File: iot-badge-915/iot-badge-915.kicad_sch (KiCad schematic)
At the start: 64 parts, among them J1 USB_C_Receptacle_USB2.0, J2 Wire ANT, J3 Conn_01x04_Male, Q1 BC847, Q2 BC847, Q3 BC847, SW1 SW_Push, SW2 SW_Push, SW3 SW_Push, SW4 SW_Push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

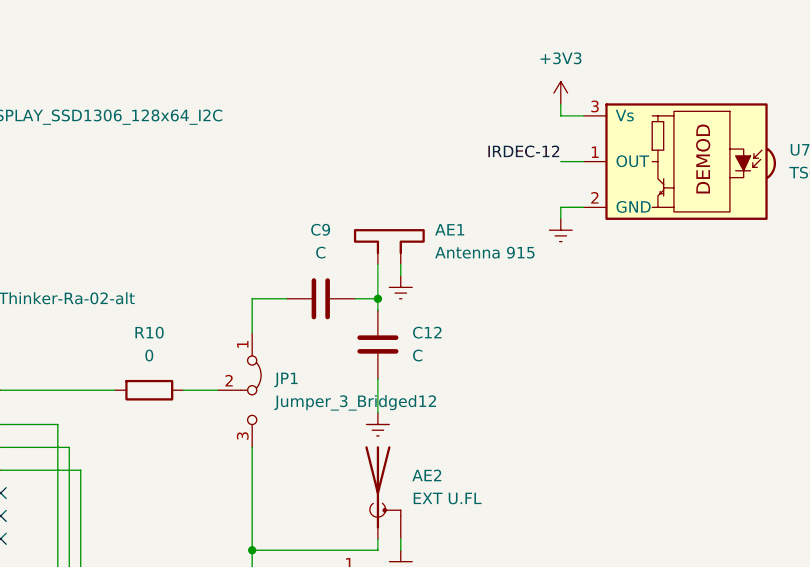
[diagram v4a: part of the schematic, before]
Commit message: added tuning cap an inductor to ant circuit
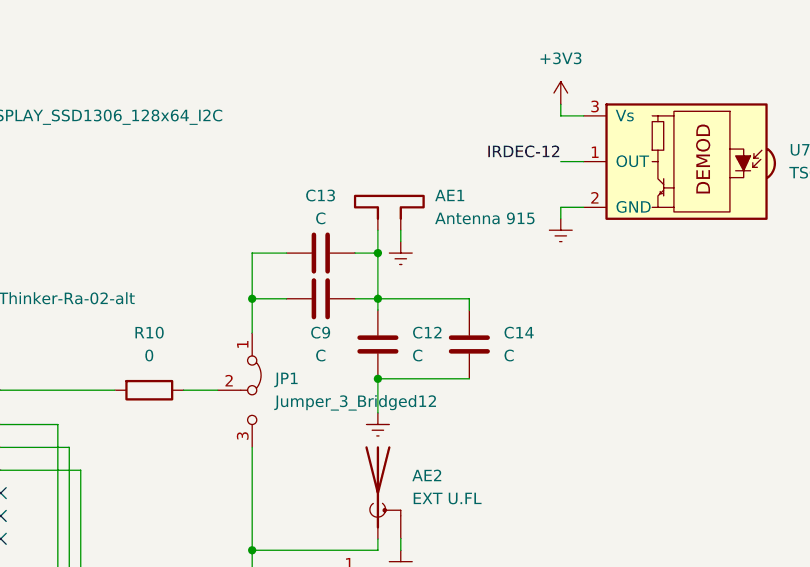
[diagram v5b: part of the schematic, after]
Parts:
- added C13, C14: C, Capacitor_SMD:C_0805_2012Metric_Pad1.18x1.45mm_HandSolder, symbol Device:C
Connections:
- net Earth: now also C14.1
- net at AE1.1, C12.2, C9.1: now also C13.1, C14.2
- net at C9.2, JP1.1 (A): now also C13.2
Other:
- moved on the sheet: AE1
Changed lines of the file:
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@@
   (junction (at 29.21 45.72) (diameter 0) (color 0 0 0 0)
   )
+  (junction (at 167.64 80.01) (diameter 0) (color 0 0 0 0)
+  )
   (junction (at 21.59 45.72) (diameter 0) (color 0 0 0 0)
   )
@@
   (junction (at 26.67 57.15) (diameter 0) (color 0 0 0 0)
   )
+  (junction (at 181.61 74.93) (diameter 0) (color 0 0 0 0)
+  )
   (junction (at 257.81 111.76) (diameter 0) (color 0 0 0 0)
   )
@@
   (junction (at 114.3 55.88) (diameter 0) (color 0 0 0 0)
   )
+  (junction (at 181.61 88.9) (diameter 0) (color 0 0 0 0)
+  )
   (junction (at 218.44 26.67) (diameter 0) (color 0 0 0 0)
   )
@@
     (stroke (width 0) (type default) (color 0 0 0 0))
   )
+  (wire (pts (xy 171.45 74.93) (xy 167.64 74.93))
+    (stroke (width 0) (type default) (color 0 0 0 0))
+  )
   (wire (pts (xy 115.57 185.42) (xy 115.57 189.23))
     (stroke (width 0) (type default) (color 0 0 0 0))
@@
     (stroke (width 0) (type default) (color 0 0 0 0))
   )
+  (wire (pts (xy 191.77 80.01) (xy 191.77 81.28))
+    (stroke (width 0) (type default) (color 0 0 0 0))
+  )
   (wire (pts (xy 115.57 176.53) (xy 118.11 176.53))
     (stroke (width 0) (type default) (color 0 0 0 0))
@@
     (stroke (width 0) (type default) (color 0 0 0 0))
   )
+  (wire (pts (xy 181.61 88.9) (xy 191.77 88.9))
+    (stroke (width 0) (type default) (color 0 0 0 0))
+  )
   (wire (pts (xy 163.83 125.73) (xy 163.83 158.75))
     (stroke (width 0) (type default) (color 0 0 0 0))
@@
     (stroke (width 0) (type default) (color 0 0 0 0))
   )
+  (wire (pts (xy 167.64 74.93) (xy 167.64 80.01))
+    (stroke (width 0) (type default) (color 0 0 0 0))
+  )
   (wire (pts (xy 171.45 80.01) (xy 167.64 80.01))
     (stroke (width 0) (type default) (color 0 0 0 0))
   )
+  (wire (pts (xy 179.07 74.93) (xy 181.61 74.93))
+    (stroke (width 0) (type default) (color 0 0 0 0))
+  )
   (wire (pts (xy 91.44 149.86) (xy 91.44 151.13))
     (stroke (width 0) (type default) (color 0 0 0 0))
   )
-  (wire (pts (xy 181.61 76.2) (xy 181.61 80.01))
+  (wire (pts (xy 181.61 72.39) (xy 181.61 74.93))
     (stroke (width 0) (type default) (color 0 0 0 0))
   )
@@
     (stroke (width 0) (type default) (color 0 0 0 0))
   )
+  (wire (pts (xy 181.61 80.01) (xy 191.77 80.01))
+    (stroke (width 0) (type default) (color 0 0 0 0))
+  )
   (wire (pts (xy 46.99 181.61) (xy 46.99 189.23))
     (stroke (width 0) (type default) (color 0 0 0 0))
@@
     (stroke (width 0) (type default) (color 0 0 0 0))
   )
-  (wire (pts (xy 184.15 76.2) (xy 184.15 77.47))
+  (wire (pts (xy 184.15 72.39) (xy 184.15 73.66))
     (stroke (width 0) (type default) (color 0 0 0 0))
   )
@@
     (stroke (width 0) (type default) (color 0 0 0 0))
   )
+  (wire (pts (xy 181.61 74.93) (xy 181.61 80.01))
+    (stroke (width 0) (type default) (color 0 0 0 0))
+  )
   (wire (pts (xy 72.39 91.44) (xy 72.39 119.38))
     (stroke (width 0) (type default) (color 0 0 0 0))
@@
   )
   (symbol (lib_id "Device:C") (at 175.26 80.01 270) (unit 1)
-    (in_bom yes) (on_board yes) (fields_autoplaced)
-    (property "Reference" "C9" (id 0) (at 175.26 72.39 90))
-    (property "Value" "C" (id 1) (at 175.26 74.93 90))
+    (in_bom yes) (on_board yes)
+    (property "Reference" "C9" (id 0) (at 175.26 83.82 90))
+    (property "Value" "C" (id 1) (at 175.26 86.36 90))
     (property "Footprint" "Capacitor_SMD:C_0805_2012Metric_Pad1.18x1.45mm_HandSolder" (id 2) (at 171.45 80.9752 0)
       (effects (font (size 1.27 1.27)) hide)
@@
     (pin "3")
   )
-  (symbol (lib_id "Device:Antenna_Dipole") (at 181.61 71.12 0) (unit 1)
+  (symbol (lib_id "Device:Antenna_Dipole") (at 181.61 67.31 0) (unit 1)
     (in_bom yes) (on_board yes) (fields_autoplaced)
-    (property "Reference" "AE1" (id 0) (at 187.96 72.3899 0)
+    (property "Reference" "AE1" (id 0) (at 187.96 68.5799 0)
       (effects (font (size 1.27 1.27)) (justify left))
     )
-    (property "Value" "Antenna 915" (id 1) (at 187.96 74.9299 0)
+    (property "Value" "Antenna 915" (id 1) (at 187.96 71.1199 0)
       (effects (font (size 1.27 1.27)) (justify left))
     )
-    (property "Footprint" "RF_PCB_Antenna:Micrel_916_ant_6" (id 2) (at 181.61 71.12 0)
+    (property "Footprint" "RF_PCB_Antenna:Micrel_916_ant_6" (id 2) (at 181.61 67.31 0)
       (effects (font (size 1.27 1.27)) hide)
     )
-    (property "Datasheet" "~" (id 3) (at 181.61 71.12 0)
+    (property "Datasheet" "~" (id 3) (at 181.61 67.31 0)
       (effects (font (size 1.27 1.27)) hide)
     )
@@
     (pin "1")
   )
+  (symbol (lib_id "Device:C") (at 175.26 74.93 270) (unit 1)
+    (in_bom yes) (on_board yes)
+    (property "Reference" "C13" (id 0) (at 175.26 68.58 90))
+    (property "Value" "C" (id 1) (at 175.26 71.12 90))
+    (property "Footprint" "Capacitor_SMD:C_0805_2012Metric_Pad1.18x1.45mm_HandSolder" (id 2) (at 171.45 75.8952 0)
+      (effects (font (size 1.27 1.27)) hide)
+    )
+    (property "Datasheet" "~" (id 3) (at 175.26 74.93 0)
+      (effects (font (size 1.27 1.27)) hide)
+    )
+    (pin "1")
+    (pin "2")
+  )
   (symbol (lib_id "Switch:SW_Push") (at 232.41 157.48 0) (unit 1)
     (in_bom yes) (on_board yes) (fields_autoplaced)
@@
     (pin "1")
   )
-  (symbol (lib_id "power:Earth") (at 184.15 77.47 0) (unit 1)
+  (symbol (lib_id "Device:C") (at 191.77 85.09 180) (unit 1)
+    (in_bom yes) (on_board yes) (fields_autoplaced)
+    (property "Reference" "C14" (id 0) (at 195.58 83.8199 0)
+      (effects (font (size 1.27 1.27)) (justify right))
+    )
+    (property "Value" "C" (id 1) (at 195.58 86.3599 0)
+      (effects (font (size 1.27 1.27)) (justify right))
+    )
+    (property "Footprint" "Capacitor_SMD:C_0805_2012Metric_Pad1.18x1.45mm_HandSolder" (id 2) (at 190.8048 81.28 0)
+      (effects (font (size 1.27 1.27)) hide)
+    )
+    (property "Datasheet" "~" (id 3) (at 191.77 85.09 0)
+      (effects (font (size 1.27 1.27)) hide)
+    )
+    (pin "1")
+    (pin "2")
+  )
+  (symbol (lib_id "power:Earth") (at 184.15 73.66 0) (unit 1)
     (in_bom yes) (on_board yes) (fields_autoplaced)
-    (property "Reference" "#PWR0121" (id 0) (at 184.15 83.82 0)
+    (property "Reference" "#PWR0121" (id 0) (at 184.15 80.01 0)
       (effects (font (size 1.27 1.27)) hide)
     )
-    (property "Value" "Earth" (id 1) (at 184.15 81.28 0)
+    (property "Value" "Earth" (id 1) (at 184.15 77.47 0)
       (effects (font (size 1.27 1.27)) hide)
     )
-    (property "Footprint" "" (id 2) (at 184.15 77.47 0)
+    (property "Footprint" "" (id 2) (at 184.15 73.66 0)
       (effects (font (size 1.27 1.27)) hide)
     )
-    (property "Datasheet" "~" (id 3) (at 184.15 77.47 0)
+    (property "Datasheet" "~" (id 3) (at 184.15 73.66 0)
       (effects (font (size 1.27 1.27)) hide)
     )
@@
       (reference "C12") (unit 1) (value "C") (footprint "Capacitor_SMD:C_0805_2012Metric_Pad1.18x1.45mm_HandSolder")
     )
+    (path "/6b88d8f5-85f6-40a1-81c4-b4f3089a30f3"
+      (reference "C13") (unit 1) (value "C") (footprint "Capacitor_SMD:C_0805_2012Metric_Pad1.18x1.45mm_HandSolder")
+    )
+    (path "/a643b7b8-93d0-49a6-9660-cedc87296a8a"
+      (reference "C14") (unit 1) (value "C") (footprint "Capacitor_SMD:C_0805_2012Metric_Pad1.18x1.45mm_HandSolder")
+    )
     (path "/2dbc282c-a4c9-44f2-b1b6-9acbf2576b02"

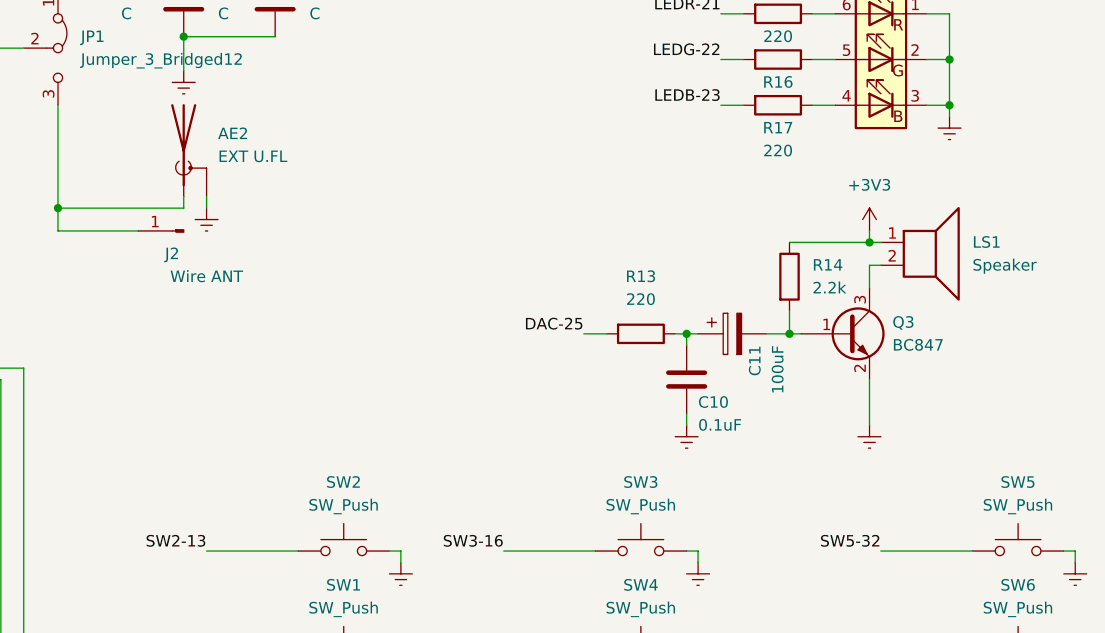
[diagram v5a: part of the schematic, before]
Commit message: added and routed audio components in 915mhz
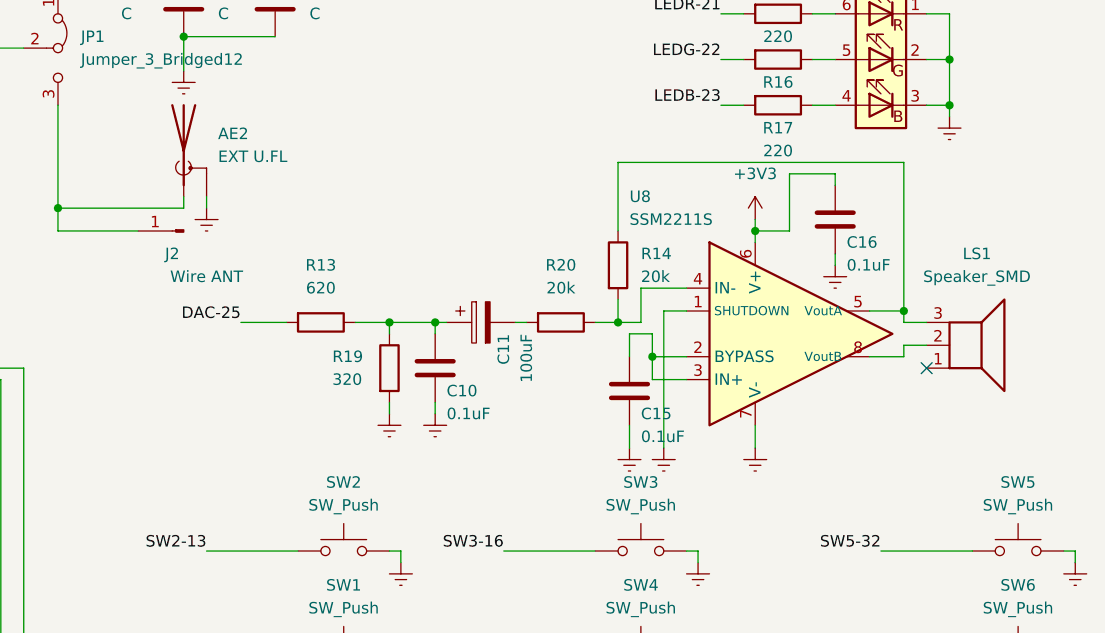
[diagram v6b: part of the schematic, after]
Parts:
- removed LS1: Speaker, Speaker_SMD:Speaker_SMD-10mmx5mm, symbol Device:Speaker
- removed Q3: BC847, Package_TO_SOT_SMD:SOT-23, symbol Transistor_BJT:BC847
- added C15, C16: 0.1uF, Capacitor_SMD:C_0805_2012Metric_Pad1.18x1.45mm_HandSolder, symbol Device:C
- added LS1: Speaker_SMD, Speaker_SMD:Speaker_SMD-5020, symbol Speaker_SMD:Speaker_SMD
- added R19: 320, Resistor_SMD:R_0805_2012Metric_Pad1.20x1.40mm_HandSolder, symbol Device:R
- added R20: 20k, Resistor_SMD:R_0805_2012Metric_Pad1.20x1.40mm_HandSolder, symbol Device:R
- added U8: SSM2211S, Package_SO:SOIC-8_3.9x4.9mm_P1.27mm, symbol Amplifier_Audio:SSM2211S
- R13: value 220 -> 620
- R14: value 2.2k -> 20k
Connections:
- net +3V3: now also C16.1, U8.6 (V+); no longer R14.1
- net Earth: now also C15.2, C16.2, R19.2, U8.1 (SHUTDOWN), U8.7 (V-)
- net at R14.2: now also R20.1, U8.4 (IN-); no longer C11.2
- net at C10.1, C11.1, R13.1: now also R19.1
- new net: LS1.3, R14.1, U8.5 (VoutA)
- new net: C15.1, U8.2 (BYPASS), U8.3 (IN+)
- new net: LS1.2, U8.8 (VoutB)
- new net: C11.2, R20.2
- no-connect marks 19 -> 20
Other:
- moved on the sheet: C10, C11, R13, R14

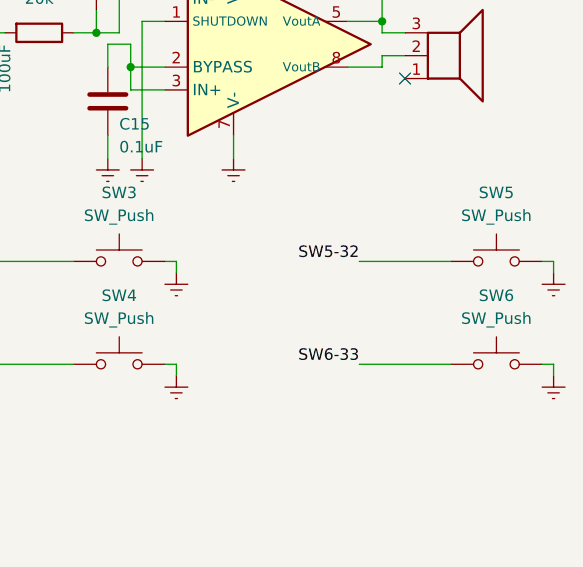
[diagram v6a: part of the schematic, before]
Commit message: added resistors to sw to protect against shorts
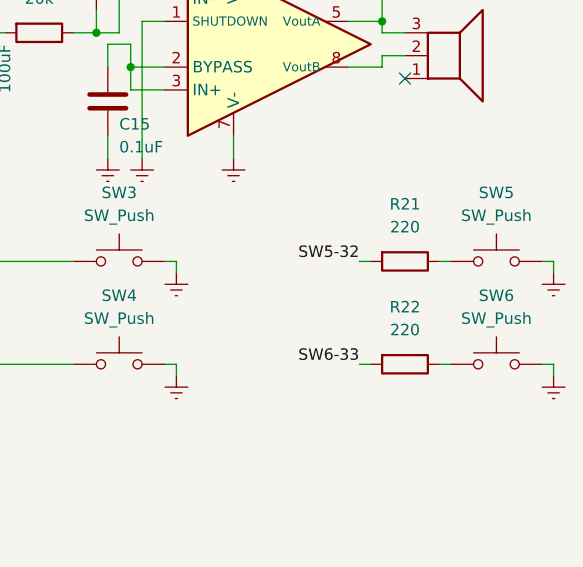
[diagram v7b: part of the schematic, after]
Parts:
- added R21, R22: 220, Resistor_SMD:R_0805_2012Metric_Pad1.20x1.40mm_HandSolder, symbol Device:R
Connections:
- net SW5-32: now also R21.2; no longer SW5.1
- net SW6-33: now also R22.2; no longer SW6.1
- new net: R21.1, SW5.1
- new net: R22.1, SW6.1
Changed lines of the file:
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@@
     (stroke (width 0) (type default) (color 0 0 0 0))
   )
-  (wire (pts (xy 259.08 157.48) (xy 269.24 157.48))
-    (stroke (width 0) (type default) (color 0 0 0 0))
-  )
   (wire (pts (xy 21.59 55.88) (xy 21.59 57.15))
     (stroke (width 0) (type default) (color 0 0 0 0))
@@
     (stroke (width 0) (type default) (color 0 0 0 0))
   )
-  (wire (pts (xy 259.08 146.05) (xy 269.24 146.05))
-    (stroke (width 0) (type default) (color 0 0 0 0))
-  )
   (wire (pts (xy 29.21 44.45) (xy 29.21 45.72))
     (stroke (width 0) (type default) (color 0 0 0 0))
@@
     (stroke (width 0) (type default) (color 0 0 0 0))
   )
+  (wire (pts (xy 267.97 146.05) (xy 269.24 146.05))
+    (stroke (width 0) (type default) (color 0 0 0 0))
+  )
   (wire (pts (xy 261.62 119.38) (xy 261.62 120.65))
     (stroke (width 0) (type default) (color 0 0 0 0))
@@
     (stroke (width 0) (type default) (color 0 0 0 0))
   )
+  (wire (pts (xy 259.08 146.05) (xy 260.35 146.05))
+    (stroke (width 0) (type default) (color 0 0 0 0))
+  )
   (wire (pts (xy 147.32 167.64) (xy 148.59 167.64))
     (stroke (width 0) (type default) (color 0 0 0 0))
@@
     (stroke (width 0) (type default) (color 0 0 0 0))
   )
+  (wire (pts (xy 267.97 157.48) (xy 269.24 157.48))
+    (stroke (width 0) (type default) (color 0 0 0 0))
+  )
   (wire (pts (xy 64.77 99.06) (xy 67.31 99.06))
     (stroke (width 0) (type default) (color 0 0 0 0))
@@
     (stroke (width 0) (type default) (color 0 0 0 0))
   )
+  (wire (pts (xy 259.08 157.48) (xy 260.35 157.48))
+    (stroke (width 0) (type default) (color 0 0 0 0))
+  )
   (wire (pts (xy 233.68 124.46) (xy 233.68 121.92))
     (stroke (width 0) (type default) (color 0 0 0 0))
@@
     (pin "1")
   )
+  (symbol (lib_id "Device:R") (at 264.16 146.05 270) (unit 1)
+    (in_bom yes) (on_board yes) (fields_autoplaced)
+    (property "Reference" "R21" (id 0) (at 264.16 139.7 90))
+    (property "Value" "220" (id 1) (at 264.16 142.24 90))
+    (property "Footprint" "Resistor_SMD:R_0805_2012Metric_Pad1.20x1.40mm_HandSolder" (id 2) (at 264.16 144.272 90)
+      (effects (font (size 1.27 1.27)) hide)
+    )
+    (property "Datasheet" "~" (id 3) (at 264.16 146.05 0)
+      (effects (font (size 1.27 1.27)) hide)
+    )
+    (pin "1")
+    (pin "2")
+  )
   (symbol (lib_id "Device:C") (at 209.55 125.73 0) (unit 1)
     (in_bom yes) (on_board yes)
@@
     (pin "2")
   )
+  (symbol (lib_id "Device:R") (at 264.16 157.48 270) (unit 1)
+    (in_bom yes) (on_board yes) (fields_autoplaced)
+    (property "Reference" "R22" (id 0) (at 264.16 151.13 90))
+    (property "Value" "220" (id 1) (at 264.16 153.67 90))
+    (property "Footprint" "Resistor_SMD:R_0805_2012Metric_Pad1.20x1.40mm_HandSolder" (id 2) (at 264.16 155.702 90)
+      (effects (font (size 1.27 1.27)) hide)
+    )
+    (property "Datasheet" "~" (id 3) (at 264.16 157.48 0)
+      (effects (font (size 1.27 1.27)) hide)
+    )
+    (pin "1")
+    (pin "2")
+  )
   (symbol (lib_id "power:Earth") (at 54.61 189.23 0) (unit 1)
     (in_bom yes) (on_board yes) (fields_autoplaced)
@@
       (reference "R20") (unit 1) (value "20k") (footprint "Resistor_SMD:R_0805_2012Metric_Pad1.20x1.40mm_HandSolder")
     )
+    (path "/4d77b265-458d-40cc-8589-30f251aa2458"
+      (reference "R21") (unit 1) (value "220") (footprint "Resistor_SMD:R_0805_2012Metric_Pad1.20x1.40mm_HandSolder")
+    )
+    (path "/f78f06ef-e42d-42b4-afa6-440b480f274f"
+      (reference "R22") (unit 1) (value "220") (footprint "Resistor_SMD:R_0805_2012Metric_Pad1.20x1.40mm_HandSolder")
+    )
     (path "/0c62dc8b-b218-44e3-b535-1d9d37793c70"

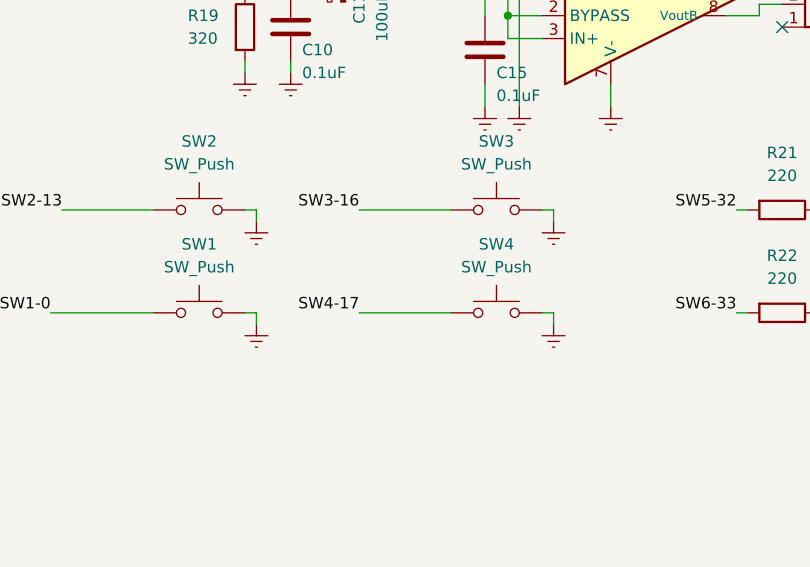
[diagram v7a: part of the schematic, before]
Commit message: added resistor to switch
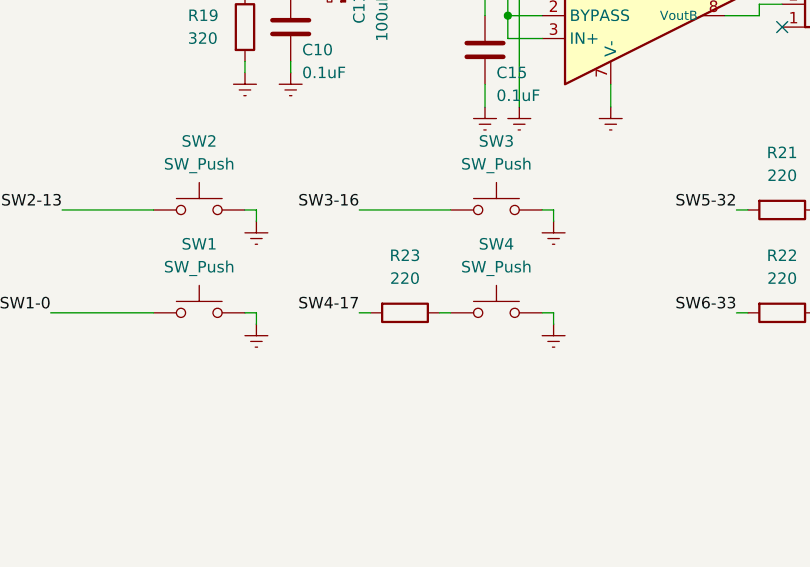
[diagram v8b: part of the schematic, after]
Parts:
- added R23: 220, Resistor_SMD:R_0805_2012Metric_Pad1.20x1.40mm_HandSolder, symbol Device:R
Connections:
- net SW4-17: now also R23.2; no longer SW4.1
- new net: R23.1, SW4.1
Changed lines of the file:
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@@
     (stroke (width 0) (type default) (color 0 0 0 0))
   )
-  (wire (pts (xy 217.17 157.48) (xy 227.33 157.48))
-    (stroke (width 0) (type default) (color 0 0 0 0))
-  )
   (wire (pts (xy 43.18 167.64) (xy 58.42 167.64))
     (stroke (width 0) (type default) (color 0 0 0 0))
@@
     (stroke (width 0) (type default) (color 0 0 0 0))
   )
+  (wire (pts (xy 217.17 157.48) (xy 218.44 157.48))
+    (stroke (width 0) (type default) (color 0 0 0 0))
+  )
   (wire (pts (xy 90.17 149.86) (xy 91.44 149.86))
     (stroke (width 0) (type default) (color 0 0 0 0))
@@
     (stroke (width 0) (type default) (color 0 0 0 0))
   )
+  (wire (pts (xy 226.06 157.48) (xy 227.33 157.48))
+    (stroke (width 0) (type default) (color 0 0 0 0))
+  )
   (wire (pts (xy 227.33 120.65) (xy 229.87 120.65))
     (stroke (width 0) (type default) (color 0 0 0 0))
@@
     (pin "2")
   )
+  (symbol (lib_id "Device:R") (at 222.25 157.48 270) (unit 1)
+    (in_bom yes) (on_board yes) (fields_autoplaced)
+    (property "Reference" "R23" (id 0) (at 222.25 151.13 90))
+    (property "Value" "220" (id 1) (at 222.25 153.67 90))
+    (property "Footprint" "Resistor_SMD:R_0805_2012Metric_Pad1.20x1.40mm_HandSolder" (id 2) (at 222.25 155.702 90)
+      (effects (font (size 1.27 1.27)) hide)
+    )
+    (property "Datasheet" "~" (id 3) (at 222.25 157.48 0)
+      (effects (font (size 1.27 1.27)) hide)
+    )
+    (pin "1")
+    (pin "2")
+  )
   (symbol (lib_id "power:Earth") (at 207.01 38.1 0) (unit 1)
     (in_bom yes) (on_board yes) (fields_autoplaced)
@@
       (reference "R22") (unit 1) (value "220") (footprint "Resistor_SMD:R_0805_2012Metric_Pad1.20x1.40mm_HandSolder")
     )
+    (path "/9c108df7-6610-49bb-b698-45fe694e32e4"
+      (reference "R23") (unit 1) (value "220") (footprint "Resistor_SMD:R_0805_2012Metric_Pad1.20x1.40mm_HandSolder")
+    )
     (path "/0c62dc8b-b218-44e3-b535-1d9d37793c70"
